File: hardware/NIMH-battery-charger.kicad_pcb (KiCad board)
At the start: 2 copper layers, 66 x 79.8 mm, 38 parts, among them J1 Conn_01x03_Pin, J3 Conn_01x01_Pin, J4 Conn_01x01_Pin, J5 Conn_01x01_Pin, J6 Conn_01x01_Pin, J7 USB_C_Receptacle_PowerOnly_6P, U1 CH32V003f4u6

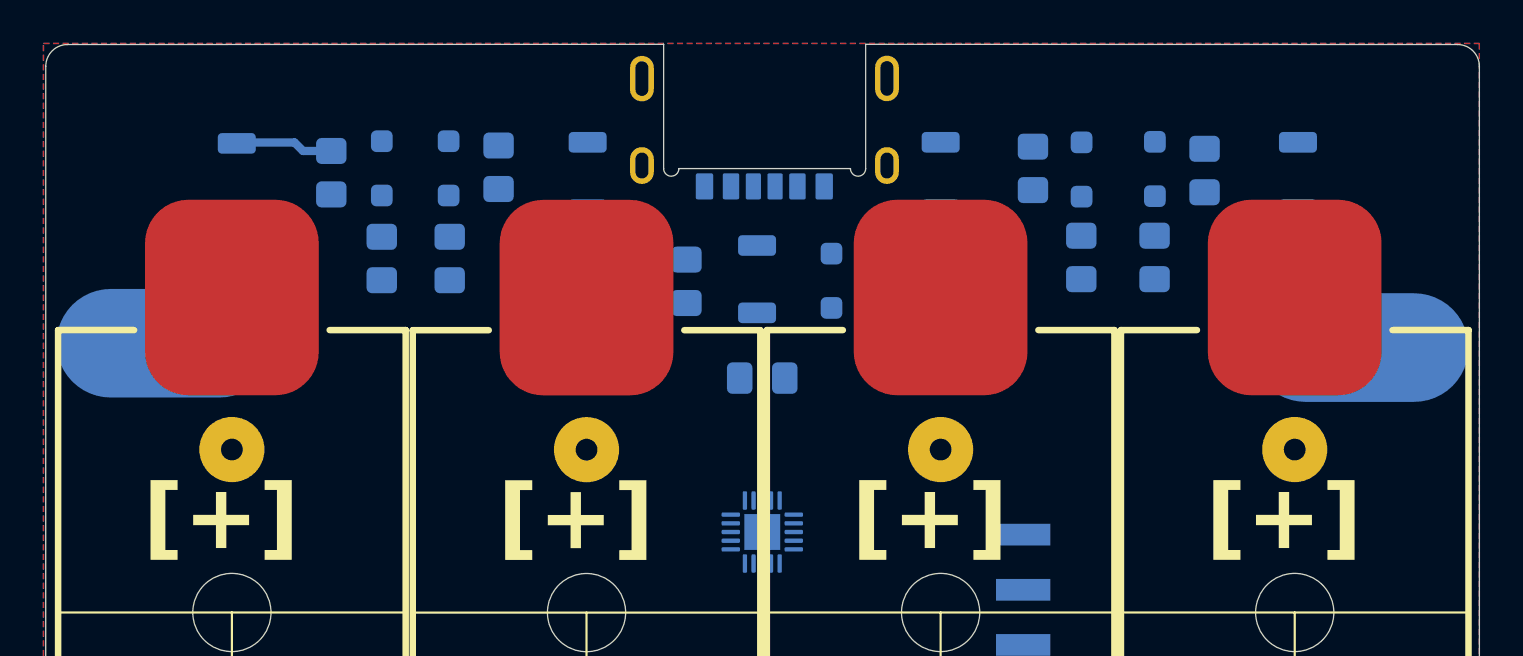
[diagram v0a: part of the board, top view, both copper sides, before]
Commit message: Started routing board
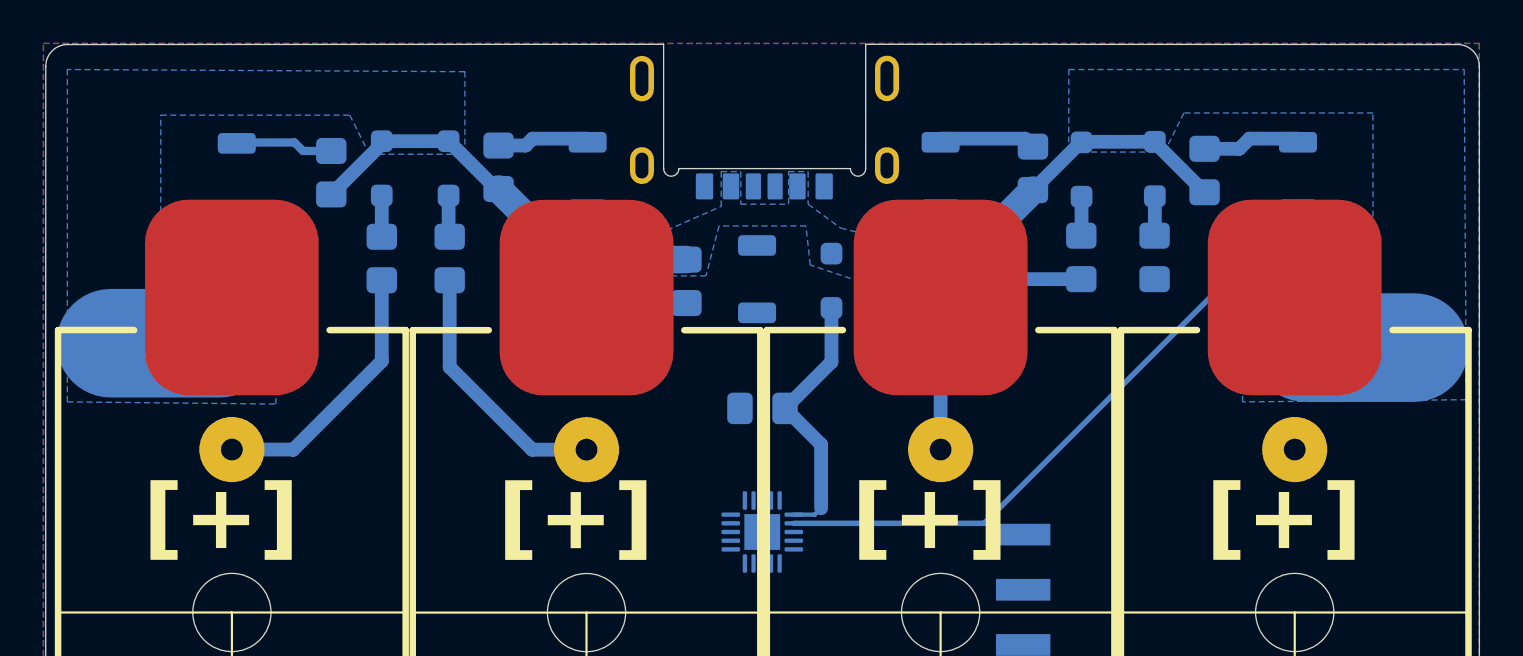
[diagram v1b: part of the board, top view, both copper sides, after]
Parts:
- moved C1 1.40 mm to (137.5, 60.8)
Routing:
- net +5V: track 0.00 -> 37.2 mm
- net /LED0: track 0.00 -> 29.2 mm
- net /ADC3: track 0.00 -> 12.5 mm
- net /ADC1: track 0.00 -> 12.3 mm
- net VDD: track 0.00 -> 12.2 mm
- net /ADC2: track 0.00 -> 11.9 mm
- net Net-(D10-A): track 0.00 -> 4.49 mm
- net Net-(D8-A): track 0.00 -> 4.40 mm
- net Net-(D6-A): track 0.00 -> 4.23 mm
- net Net-(D2-K): track 0.00 -> 1.92 mm
- net Net-(D1-K): track 0.00 -> 1.90 mm
- net Net-(D4-K): track 0.00 -> 1.83 mm
- net Net-(D3-K): track 0.00 -> 1.80 mm
- added copper zone on B.Cu, net +5V

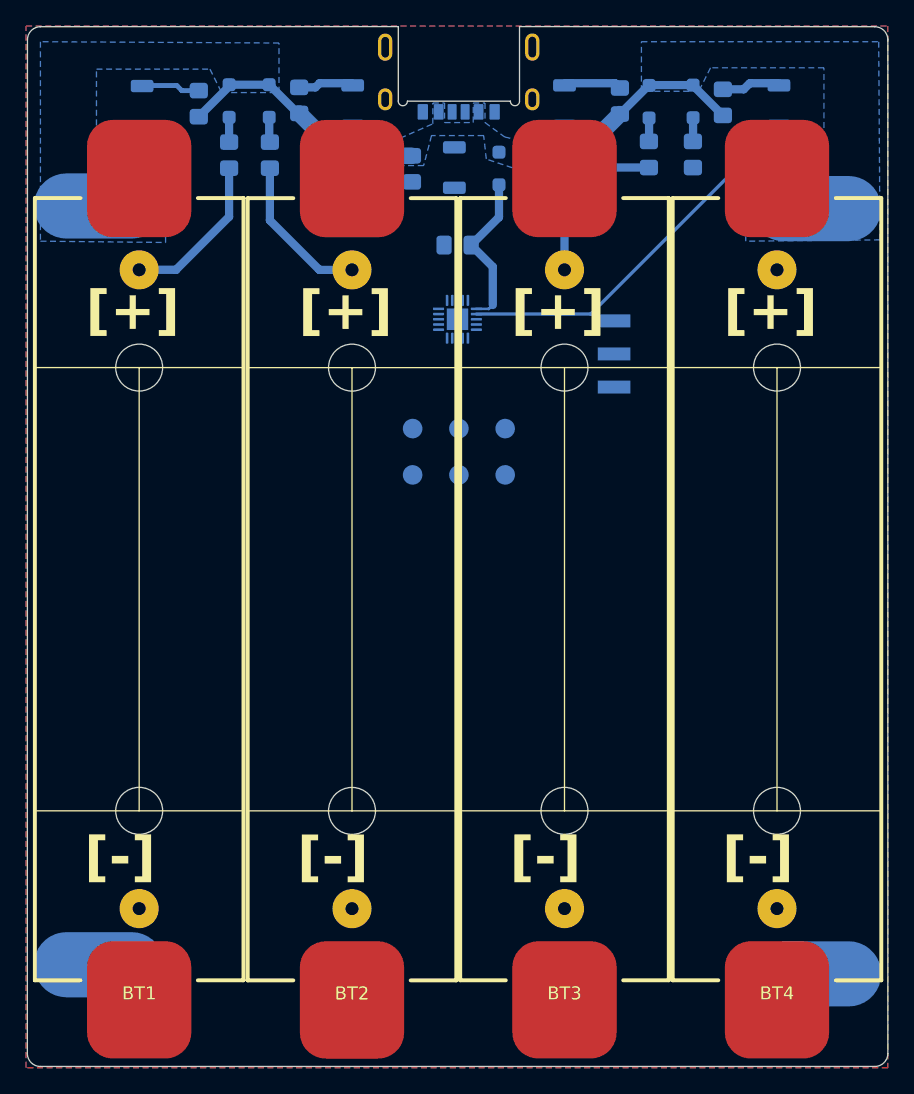
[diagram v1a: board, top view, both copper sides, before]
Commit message: Completed routing board
Created gergers for JLCPCB
Added mounting holes
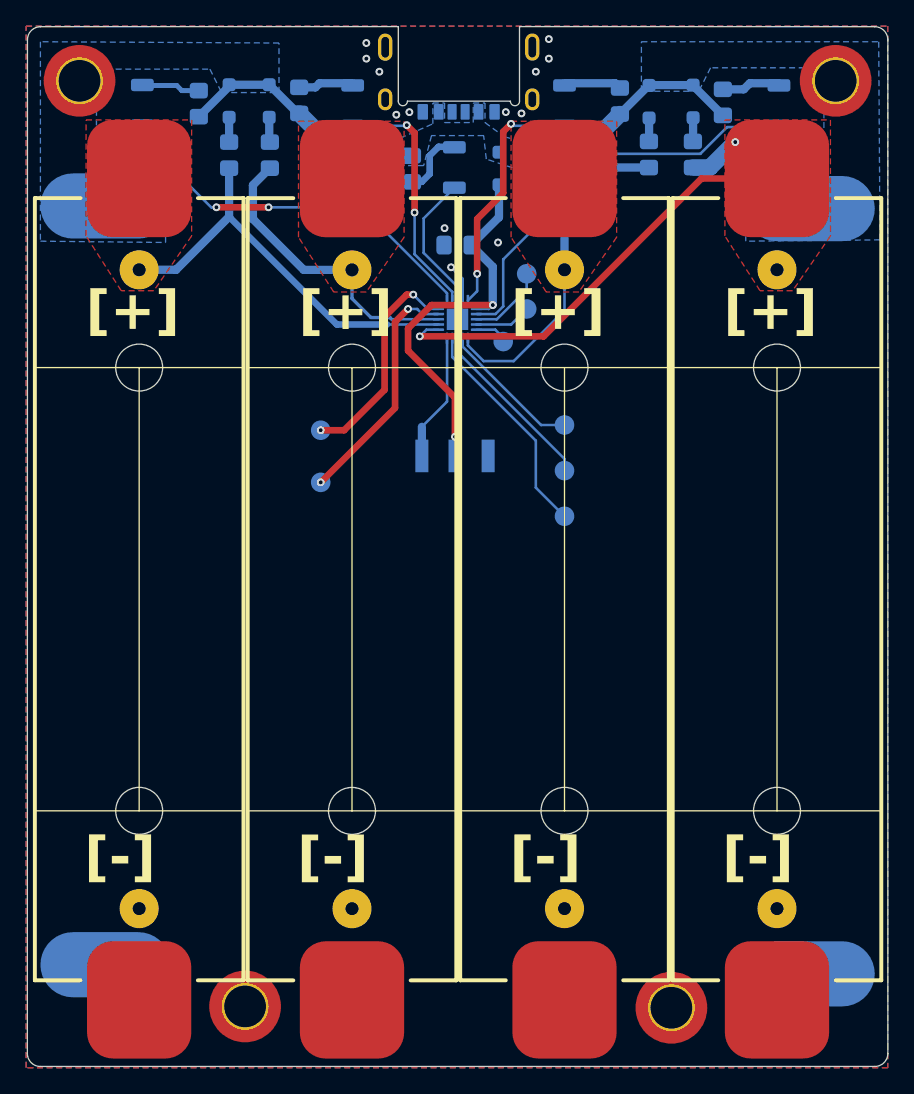
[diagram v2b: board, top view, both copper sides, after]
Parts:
- added H1: MountingHole, MountingHole:MountingHole_3.2mm_M3_ISO14580_Pad_TopOnly, F.Cu at (108.5, 48.2)
- added H2: MountingHole, MountingHole:MountingHole_3.2mm_M3_ISO14580_Pad_TopOnly, F.Cu at (166.5, 48.2)
- added H3: MountingHole, MountingHole:MountingHole_3.2mm_M3_ISO14580_Pad_TopOnly, F.Cu at (121.2, 119.2)
- added H4: MountingHole, MountingHole:MountingHole_3.2mm_M3_ISO14580_Pad_TopOnly, F.Cu at (153.9, 119.3)
- added TP7: TestPoint, TestPoint:TestPoint_Pad_D1.5mm, B.Cu at (127.0, 79.0)
- added TP8: TestPoint, TestPoint:TestPoint_Pad_D1.5mm, B.Cu at (127.0, 75.0)
- added kibuzzard-672F4251: G***, kibuzzard-672F4251, B.Cu at (117.3, 74.9)
- added kibuzzard-672F425B: G***, kibuzzard-672F425B, B.Cu at (117.4, 79.1)
- added kibuzzard-672F427A: G***, kibuzzard-672F427A, B.Cu at (134.6, 95.8)
- moved J1 22.2 mm to (137.3, 82.5), turned to -90 degrees
- moved TP2 12.8 mm to (142.8, 65.7)
- moved TP5 12.1 mm to (145.7, 78.1)
- moved TP6 12.1 mm to (145.7, 81.6)
- moved TP1 12.0 mm to (142.8, 63.0)
- moved TP4 8.96 mm to (145.7, 74.6)
- moved TP3 7.49 mm to (141.0, 68.2)
- moved J3 0.50 mm to (164.5, 58.0)
- moved J4 0.50 mm to (164.5, 116.7)
- moved J5 0.50 mm to (110.5, 57.8)
- moved J6 0.50 mm to (110.5, 116.0)
- moved D5 0.08 mm to (113.3, 50.1)
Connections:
- U1 pad 11: /ADC1 -> /ADC3
- U1 pad 16: /ADC2 -> /ADC4
- U1 pad 17: /ADC3 -> /ADC1
- U1 pad 18: /ADC4 -> /ADC2
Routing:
- net /ADC4: track 0.00 -> 38.1 mm, vias 0 -> 2
- net /LED1: track 0.00 -> 29.8 mm, vias 0 -> 2
- net /ADC1: track 12.3 -> 32.2 mm
- net /LED4: track 0.00 -> 19.1 mm, vias 0 -> 2
- net /LED2: track 0.00 -> 19.1 mm, vias 0 -> 2
- net /UART_TX: track 0.00 -> 18.6 mm, vias 0 -> 2
- net VDD: track 12.2 -> 30.7 mm, vias 0 -> 2
- net Net-(U1-PC7_MISO): track 0.00 -> 17.2 mm
- net /UART_RX: track 0.00 -> 17.1 mm, vias 0 -> 2
- net Net-(U1-PC6_MOSI): track 0.00 -> 13.6 mm
- net /ADC3: track 12.5 -> 25.7 mm
- net /ADC2: track 11.9 -> 23.2 mm
- net Net-(U1-PC5_SCK): track 0.00 -> 10.9 mm
- net /LED3: track 0.00 -> 10.7 mm
- net /SWIO: track 0.00 -> 9.83 mm
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- added copper zone on F.Cu, net /ADC1
- added copper zone on F.Cu, net /ADC2
- added copper zone on F.Cu, net /ADC3
- added copper zone on F.Cu, net /ADC4
